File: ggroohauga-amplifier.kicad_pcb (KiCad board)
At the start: 2 copper layers, 90 x 31 mm, 9 parts

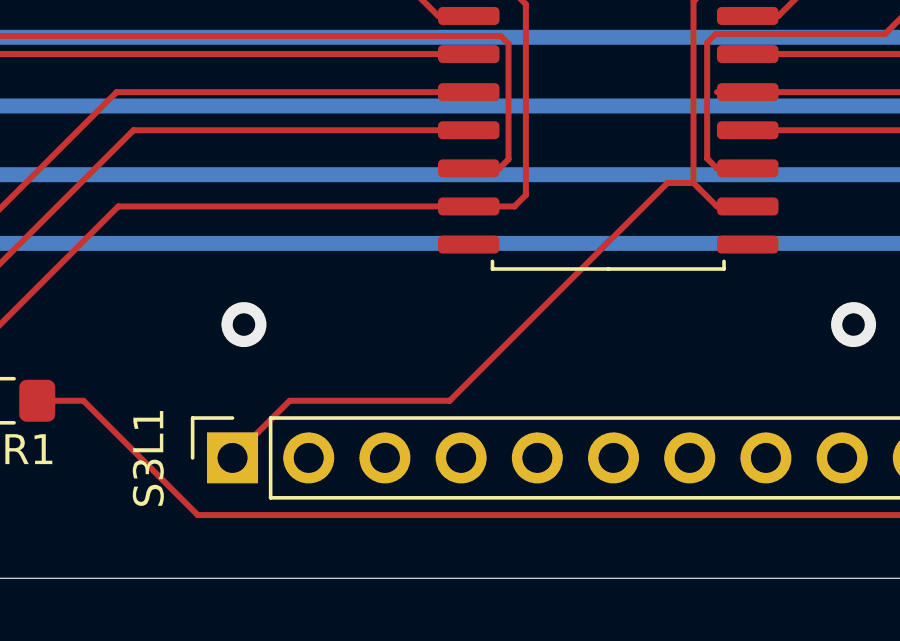
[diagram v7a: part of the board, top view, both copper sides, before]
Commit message: Add 4ch digital isolator to the bridge PCB
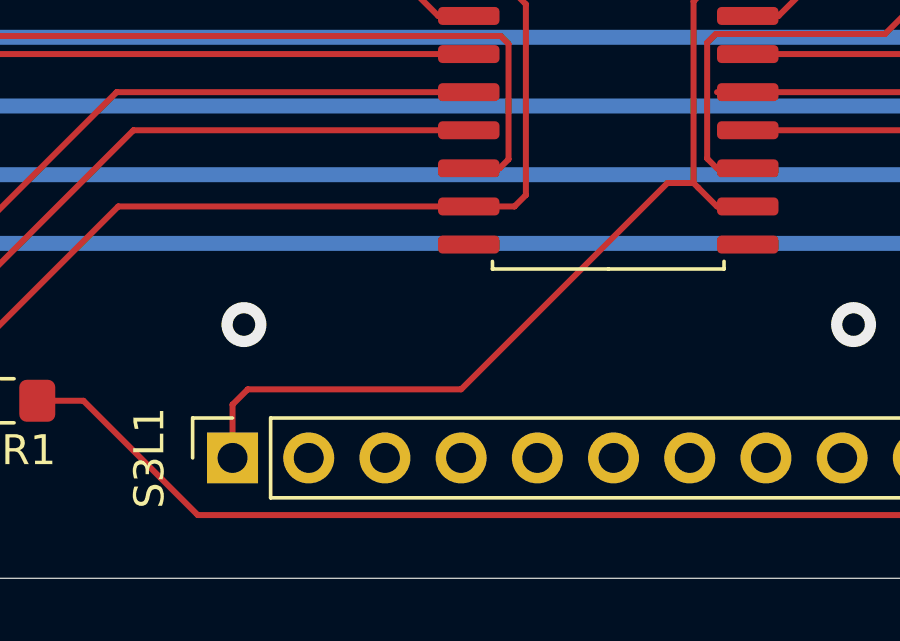
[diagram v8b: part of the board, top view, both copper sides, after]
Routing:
- net +3.3V: track 31.5 -> 32.6 mm
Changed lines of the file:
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@@
+	)
+	(segment
+		(start 82.042 75.184)
+		(end 81.534 75.692)
+		(width 0.2)
+		(layer "F.Cu")
+		(net 21)
+	)
+	(segment
+		(start 89.154 75.184)
+		(end 82.042 75.184)
+		(width 0.2)
+		(layer "F.Cu")
+		(net 21)
 	)
 	(segment
@@
 		(start 98.708 61.468)
 		(end 97.683001 61.468)
+		(width 0.2)
+		(layer "F.Cu")
+		(net 21)
+	)
+	(segment
+		(start 96.901 68.305999)
+		(end 96.032001 68.305999)
 		(width 0.2)
 		(layer "F.Cu")
@@
 	)
 	(segment
-		(start 88.773 75.565)
-		(end 83.439 75.565)
+		(start 96.032001 68.305999)
+		(end 89.154 75.184)
 		(width 0.2)
 		(layer "F.Cu")
@@
 	)
 	(segment
-		(start 96.901 68.305999)
-		(end 96.032001 68.305999)
+		(start 81.534 75.692)
+		(end 81.534 77.47)
 		(width 0.2)
 		(layer "F.Cu")
@@
 		(width 0.2)
 		(layer "F.Cu")
-		(net 21)
-	)
-	(segment
-		(start 96.032001 68.305999)
-		(end 88.773 75.565)
-		(width 0.2)
-		(layer "F.Cu")
-		(net 21)
-	)
-	(segment
-		(start 83.439 75.565)
-		(end 81.534 77.47)
-		(width 0.2)
-		(layer "F.Cu")
